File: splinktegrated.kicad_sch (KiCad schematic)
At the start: 160 parts, among them J1 USB_C_Receptacle_USB2.0, J10 NA_Ribbon, J13 Conn_01x01_Socket, J14 Cirque, J15 Conn_01x01_Socket, J16 Conn_01x01_Socket, J17 Conn_01x01_Socket, J18 USB_C_Receptacle_USB2.0, J19 Conn_01x01_Socket, J20 Conn_01x01_Socket, J5 Conn_01x02, J7 NA_trackball, J8 NA_Ribbon, J9 NA_RGB, Q4 AO3401A, Q5 AO3401A, SW2 NA_SW_SPST, SW9001 NA_SW_SPST, U1 RP2040, U2 USBLC6-2P6, U3 XC6210B332MR-G, U4 USBLC6-2P6, U5 W25Q128JVS, U6 74LVC1T45, Y1 Crystal_GND24

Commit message: routing
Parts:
- removed D6, D7: D_TVS, Diode_SMD:D_SOD-523, symbol Device:D_TVS
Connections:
- net D13: now also D3.2 (A2)
- net D14: now also D4.2 (A2)
- net GND: now also D10.1 (A1), D11.1 (A1), D12.1 (A1), D13.1 (A1), D14.1 (A1), D15.1 (A1), D16.2 (A2), D17.2 (A2), D18.2 (A2), D19.2 (A2), D20.2 (A2), D21.2 (A2), D3.1 (A1), D4.1 (A1), D5.2 (A2), D5085.2 (A2), D8.2 (A2), D9.2 (A2)
- net col1_l: now also D9.1 (A1)
- net col2_l: now also D5.1 (A1)
- net col3_l: now also D18.1 (A1)
- net col4_l: now also D17.1 (A1)
- net col5_l: now also D21.1 (A1)
- net col6_l: now also D20.1 (A1)
- net miso_l: now also D12.2 (A2)
- net mosi_l: now also D15.2 (A2)
- net rgb_3v3: now also D13.2 (A2)
- net row1_l: now also D10.2 (A2)
- net row2_l: now also D8.1 (A1)
- net row3_l: now also D19.1 (A1)
- net row4_l: now also D16.1 (A1)
- net row5_l: now also D5085.1 (A1)
- net sc_l: now also D11.2 (A2)
- net ss_l: now also D14.2 (A2)
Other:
- moved on the sheet: D10, D11, D12, D13, D14, D15, D16, D17, D18, D19, D20, D21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

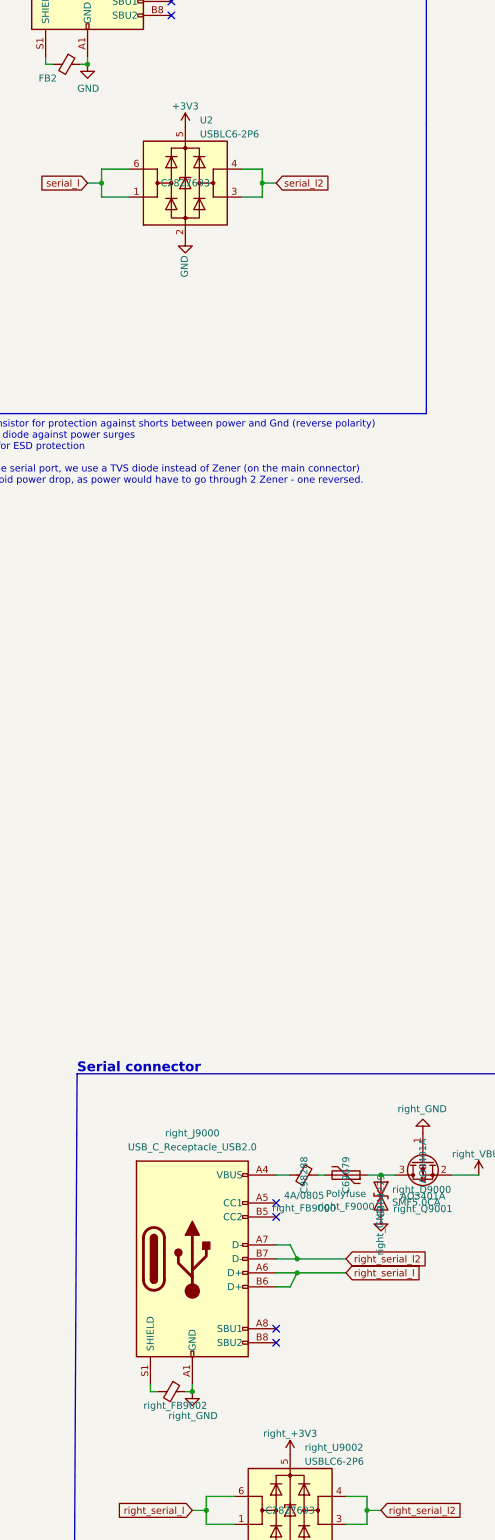
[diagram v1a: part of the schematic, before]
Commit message: vbus on serial esd pin
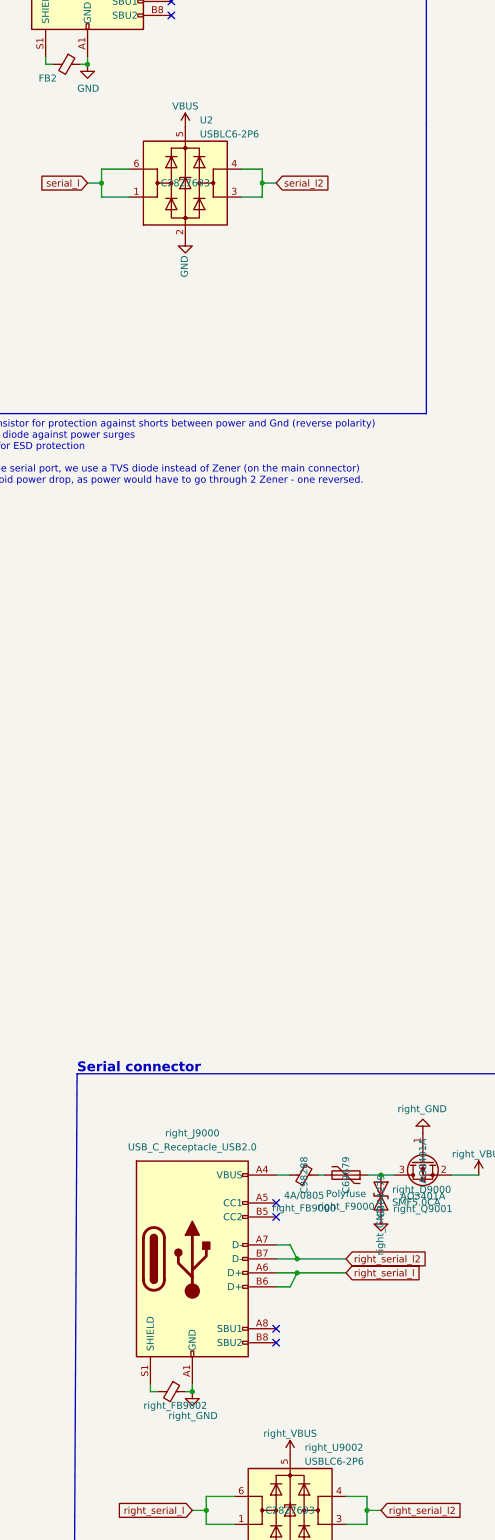
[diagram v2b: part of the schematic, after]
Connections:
- net +3V3: no longer U2.5 (VBUS)
- net VBUS: now also U2.5 (VBUS)
- net right_+3V3: no longer right_U9002.5 (VBUS)
- net right_VBUS: now also right_U9002.5 (VBUS)
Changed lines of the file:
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@@
 	)
 	(symbol
+		(lib_id "power:VBUS")
+		(at -132.08 318.77 0)
+		(unit 1)
+		(exclude_from_sim no)
+		(in_bom yes)
+		(on_board yes)
+		(dnp no)
+		(property "Reference" "#PWR0116"
+			(at -132.08 322.58 0)
+			(effects
+				(font
+					(size 1.27 1.27)
+				)
+				(hide yes)
+			)
+		)
+		(property "Value" "right_VBUS"
+			(at -132.08 314.96 0)
+			(effects
+				(font
+					(size 1.27 1.27)
+				)
+			)
+		)
+		(property "Footprint" ""
+			(at -132.08 318.77 0)
+			(effects
+				(font
+					(size 1.27 1.27)
+				)
+				(hide yes)
+			)
+		)
+		(property "Datasheet" ""
+			(at -132.08 318.77 0)
+			(effects
+				(font
+					(size 1.27 1.27)
+				)
+				(hide yes)
+			)
+		)
+		(property "Description" ""
+			(at -132.08 318.77 0)
+			(effects
+				(font
+					(size 1.27 1.27)
+				)
+				(hide yes)
+			)
+		)
+		(pin "1"
+		)
+		(instances
+			(project "splinktegrated"
+				(path "/7353e96a-343a-4876-b497-b1d205a14d97"
+					(reference "#PWR0116")
+					(unit 1)
+				)
+			)
+		)
+	)
+	(symbol
 		(lib_id "Connector:Conn_01x14_Female")
 		(at 415.29 290.83 0)
@@
 	)
 	(symbol
-		(lib_id "power:+3.3V")
-		(at -151.13 77.47 0)
-		(unit 1)
-		(exclude_from_sim no)
-		(in_bom yes)
-		(on_board yes)
-		(dnp no)
-		(property "Reference" "#PWR030"
-			(at -151.13 81.28 0)
-			(effects
-				(font
-					(size 1.27 1.27)
-				)
-				(hide yes)
-			)
-		)
-		(property "Value" "+3V3"
-			(at -151.13 73.66 0)
-			(effects
-				(font
-					(size 1.27 1.27)
-				)
-			)
-		)
-		(property "Footprint" ""
-			(at -151.13 77.47 0)
-			(effects
-				(font
-					(size 1.27 1.27)
-				)
-				(hide yes)
-			)
-		)
-		(property "Datasheet" ""
-			(at -151.13 77.47 0)
-			(effects
-				(font
-					(size 1.27 1.27)
-				)
-				(hide yes)
-			)
-		)
-		(property "Description" ""
-			(at -151.13 77.47 0)
-			(effects
-				(font
-					(size 1.27 1.27)
-				)
-				(hide yes)
-			)
-		)
-		(pin "1"
-		)
-		(instances
-			(project "splinktegrated"
-				(path "/7353e96a-343a-4876-b497-b1d205a14d97"
-					(reference "#PWR030")
-					(unit 1)
-				)
-			)
-		)
-	)
-	(symbol
 		(lib_id "Device:D_Schottky")
 		(at -24.13 25.4 180)
@@
 	(symbol
 		(lib_id "power:+3.3V")
-		(at -132.08 318.77 0)
-		(unit 1)
-		(exclude_from_sim no)
-		(in_bom yes)
-		(on_board yes)
-		(dnp no)
-		(property "Reference" "#PWR052"
-			(at -132.08 322.58 0)
-			(effects
-				(font
-					(size 1.27 1.27)
-				)
-				(hide yes)
-			)
-		)
-		(property "Value" "right_+3V3"
-			(at -132.08 314.96 0)
-			(effects
-				(font
-					(size 1.27 1.27)
-				)
-			)
-		)
-		(property "Footprint" ""
-			(at -132.08 318.77 0)
-			(effects
-				(font
-					(size 1.27 1.27)
-				)
-				(hide yes)
-			)
-		)
-		(property "Datasheet" ""
-			(at -132.08 318.77 0)
-			(effects
-				(font
-					(size 1.27 1.27)
-				)
-				(hide yes)
-			)
-		)
-		(property "Description" ""
-			(at -132.08 318.77 0)
-			(effects
-				(font
-					(size 1.27 1.27)
-				)
-				(hide yes)
-			)
-		)
-		(pin "1"
-		)
-		(instances
-			(project "splinktegrated"
-				(path "/7353e96a-343a-4876-b497-b1d205a14d97"
-					(reference "#PWR052")
-					(unit 1)
-				)
-			)
-		)
-	)
-	(symbol
-		(lib_id "power:+3.3V")
 		(at 332.74 129.54 270)
 		(unit 1)
@@
 					(unit 1)
 				)
+			)
+		)
+	)
+	(symbol
+		(lib_id "power:VBUS")
+		(at -151.13 77.47 0)
+		(unit 1)
+		(exclude_from_sim no)
+		(in_bom yes)
+		(on_board yes)
+		(dnp no)
+		(property "Reference" "#PWR0115"
+			(at -151.13 81.28 0)
+			(effects
+				(font
+					(size 1.27 1.27)
+				)
+				(hide yes)
+			)
+		)
+		(property "Value" "VBUS"
+			(at -151.13 73.66 0)
+			(effects
+				(font
+					(size 1.27 1.27)
+				)
+			)
+		)
+		(property "Footprint" ""
+			(at -151.13 77.47 0)
+			(effects
+				(font
+					(size 1.27 1.27)
+				)
+				(hide yes)
+			)
+		)
+		(property "Datasheet" ""
+			(at -151.13 77.47 0)
+			(effects
+				(font
+					(size 1.27 1.27)
+				)
+				(hide yes)
+			)
+		)
+		(property "Description" ""
+			(at -151.13 77.47 0)
+			(effects
+				(font
+					(size 1.27 1.27)
+				)
+				(hide yes)
+			)
+		)
+		(pin "1"
+		)
+		(instances
+			(project "splinktegrated"
+				(path "/7353e96a-343a-4876-b497-b1d205a14d97"
+					(reference "#PWR0115")
+					(unit 1)
+				)

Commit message: silkscreen
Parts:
- added H5008, H5009, H5010, H5011, H5012, H5013, H5014, H5015: NA_M4, local-libraries:mousebite, symbol Mechanical:MountingHole_Pad
- added H5016, H5017, H5020, H5021, H5022, H5023, H5024, H5025, H5026, H5027: NA_M4, local-libraries:mousebite_small, symbol Mechanical:MountingHole_Pad
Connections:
- net GND: now also D10.2 (A2), D11.2 (A2), D12.2 (A2), D14.2 (A2), D15.2 (A2); no longer D10.1 (A1), D11.1 (A1), D12.1 (A1), D14.1 (A1), D15.1 (A1)
- net miso_l: now also D12.1 (A1); no longer D12.2 (A2)
- net mosi_l: now also D15.1 (A1); no longer D15.2 (A2)
- net right_GND: now also D22.2 (A2), D23.2 (A2), D24.2 (A2), D25.2 (A2), D28.2 (A2), D29.2 (A2); no longer D22.1 (A1), D23.1 (A1), D24.1 (A1), D25.1 (A1), D28.1 (A1), D29.1 (A1)
- net right_MISO_l: now also D23.1 (A1); no longer D23.2 (A2)
- net right_MOSI_l: now also D29.1 (A1); no longer D29.2 (A2)
- net right_rgb_3v3: now also D28.1 (A1); no longer D28.2 (A2)
- net right_row1_l: now also D22.1 (A1); no longer D22.2 (A2)
- net right_sc_l: now also D24.1 (A1); no longer D24.2 (A2)
- net right_ss_l: now also D25.1 (A1); no longer D25.2 (A2)
- net row1_l: now also D10.1 (A1); no longer D10.2 (A2)
- net sc_l: now also D11.1 (A1); no longer D11.2 (A2)
- net ss_l: now also D14.1 (A1); no longer D14.2 (A2)
- no-connect marks 28 -> 46
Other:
- note added: "Mouse bites"
- moved on the sheet: D10, D11, D12, D14, D15, D22, D23, D24, D25, D28
